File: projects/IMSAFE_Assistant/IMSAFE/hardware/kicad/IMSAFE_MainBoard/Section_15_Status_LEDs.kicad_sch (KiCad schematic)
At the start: 5 parts

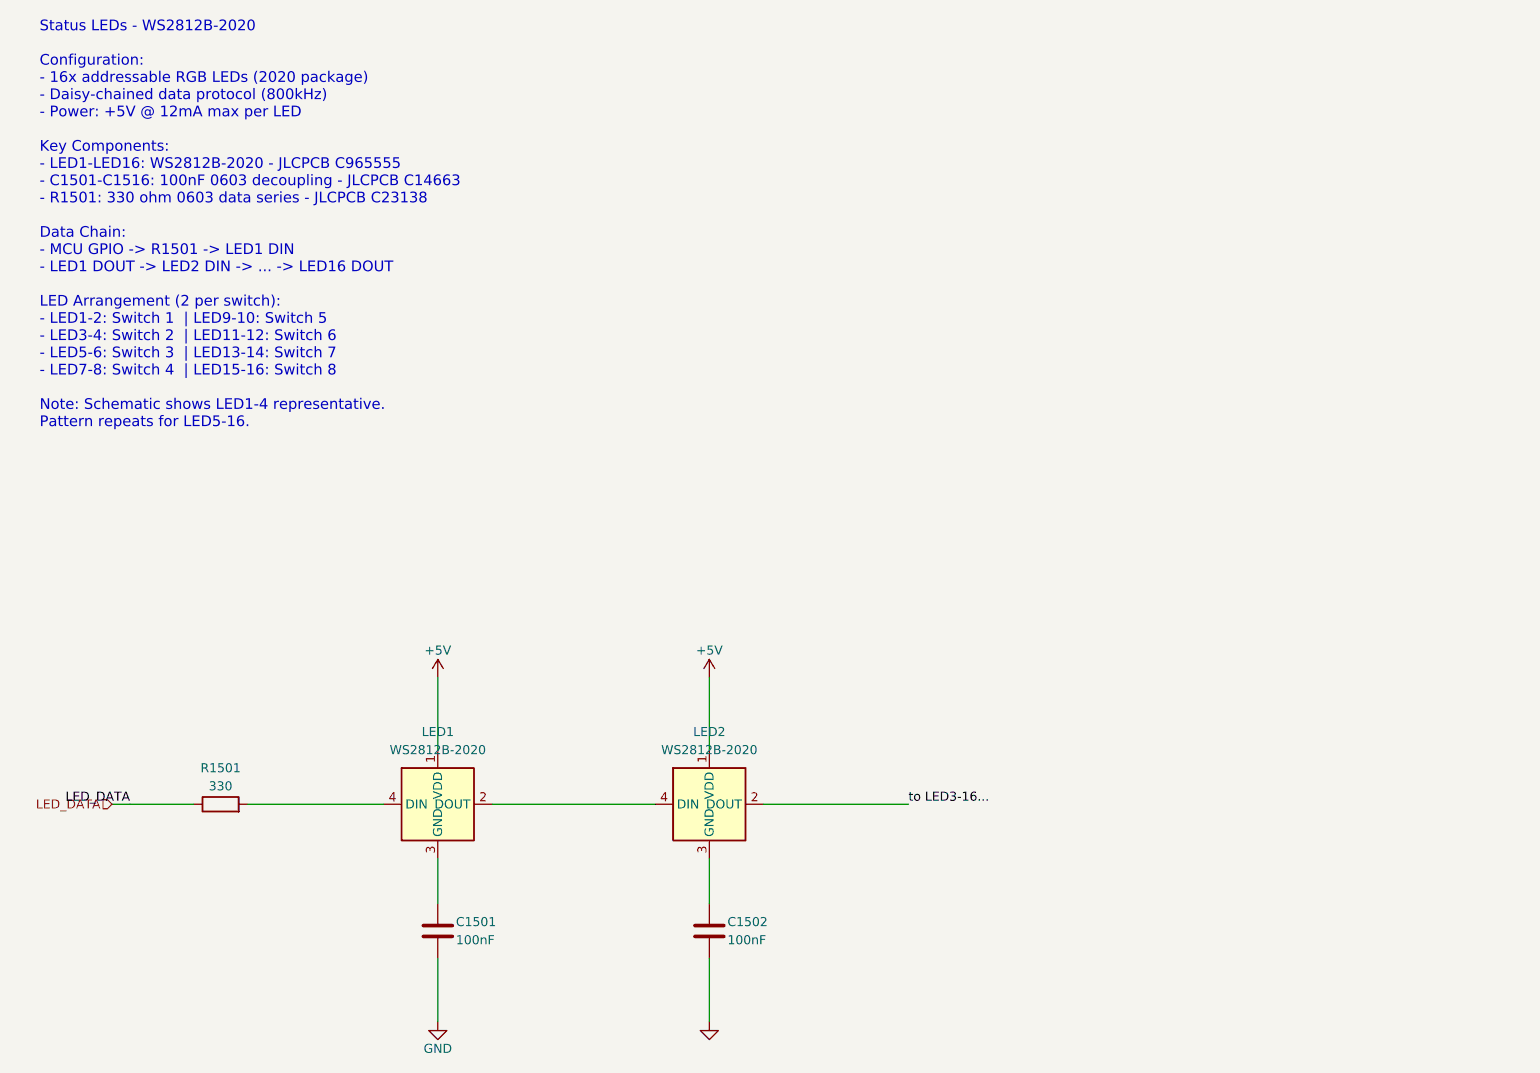
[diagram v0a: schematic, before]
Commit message: Update KiCad schematics and add analysis files
- Update all MainBoard schematic sections with component placement
- Add ERC reports and analysis scripts for schematic validation
- Update Radar Interface and SwitchLED Board projects
- Sync KiCad project files with latest session changes

Co-Authored-By: Claude Opus 4.5 <noreply@anthropic.com>
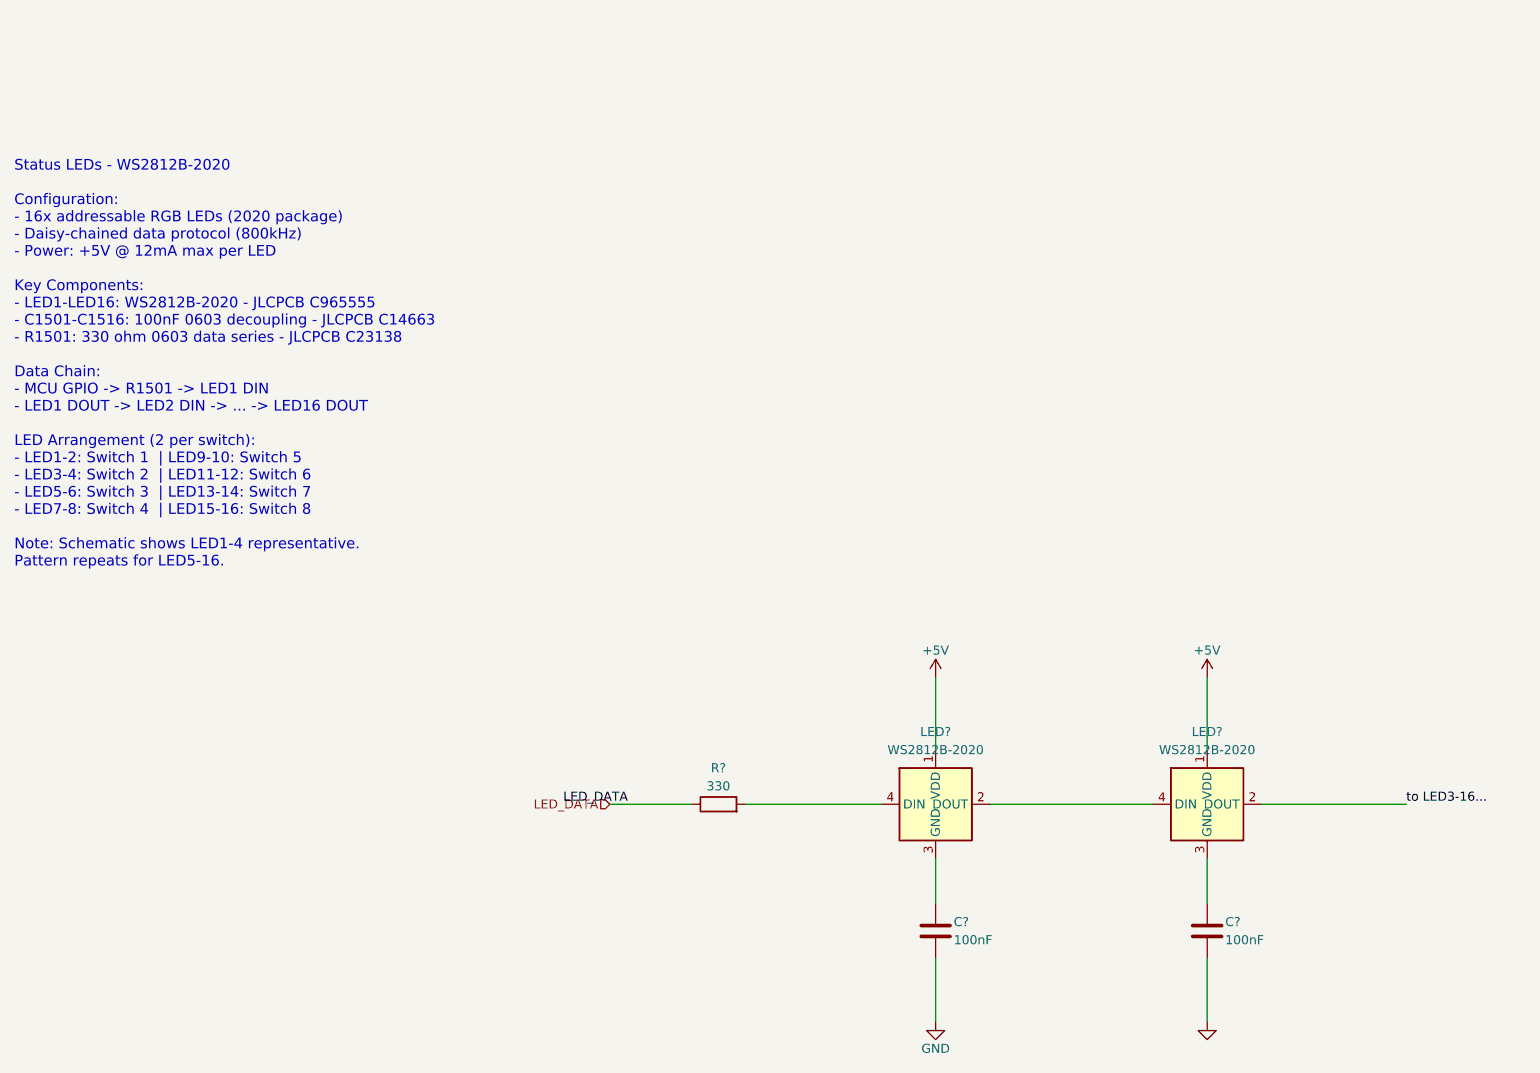
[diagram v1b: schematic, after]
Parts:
- removed C1501, C1502: 100nF, Capacitor_SMD:C_0603_1608Metric, symbol Device:C
- removed LED1, LED2: WS2812B-2020, LED_SMD:LED_WS2812B-2020_2.0x2.0mm, symbol LED:WS2812B-2020
- removed R1501: 330, Resistor_SMD:R_0603_1608Metric, symbol Device:R
- added C? (x2): 100nF, Capacitor_SMD:C_0603_1608Metric, symbol Device:C
- added LED? (x2): WS2812B-2020, LED_SMD:LED_WS2812B-2020_2.0x2.0mm, symbol LED:WS2812B-2020
- added R?: 330, Resistor_SMD:R_0603_1608Metric, symbol Device:R
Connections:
- net +5V: now also LED?.1 (VDD), LED?.1 (VDD)
- net GND: now also C?.2, C?.2
- net LED_DATA: now also R?.1
- net to LED3-16...: now also LED?.2 (DOUT)
- new net: LED?.4 (DIN), R?.2
- new net: LED?.2 (DOUT), LED?.4 (DIN)
- new net: C?.1, LED?.3 (GND) (x2)
